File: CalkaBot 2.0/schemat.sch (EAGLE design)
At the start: 52 parts, among them IC1 TB6612FNG, IC2 LM339D, IC3 7806DT, Q1 16MHz

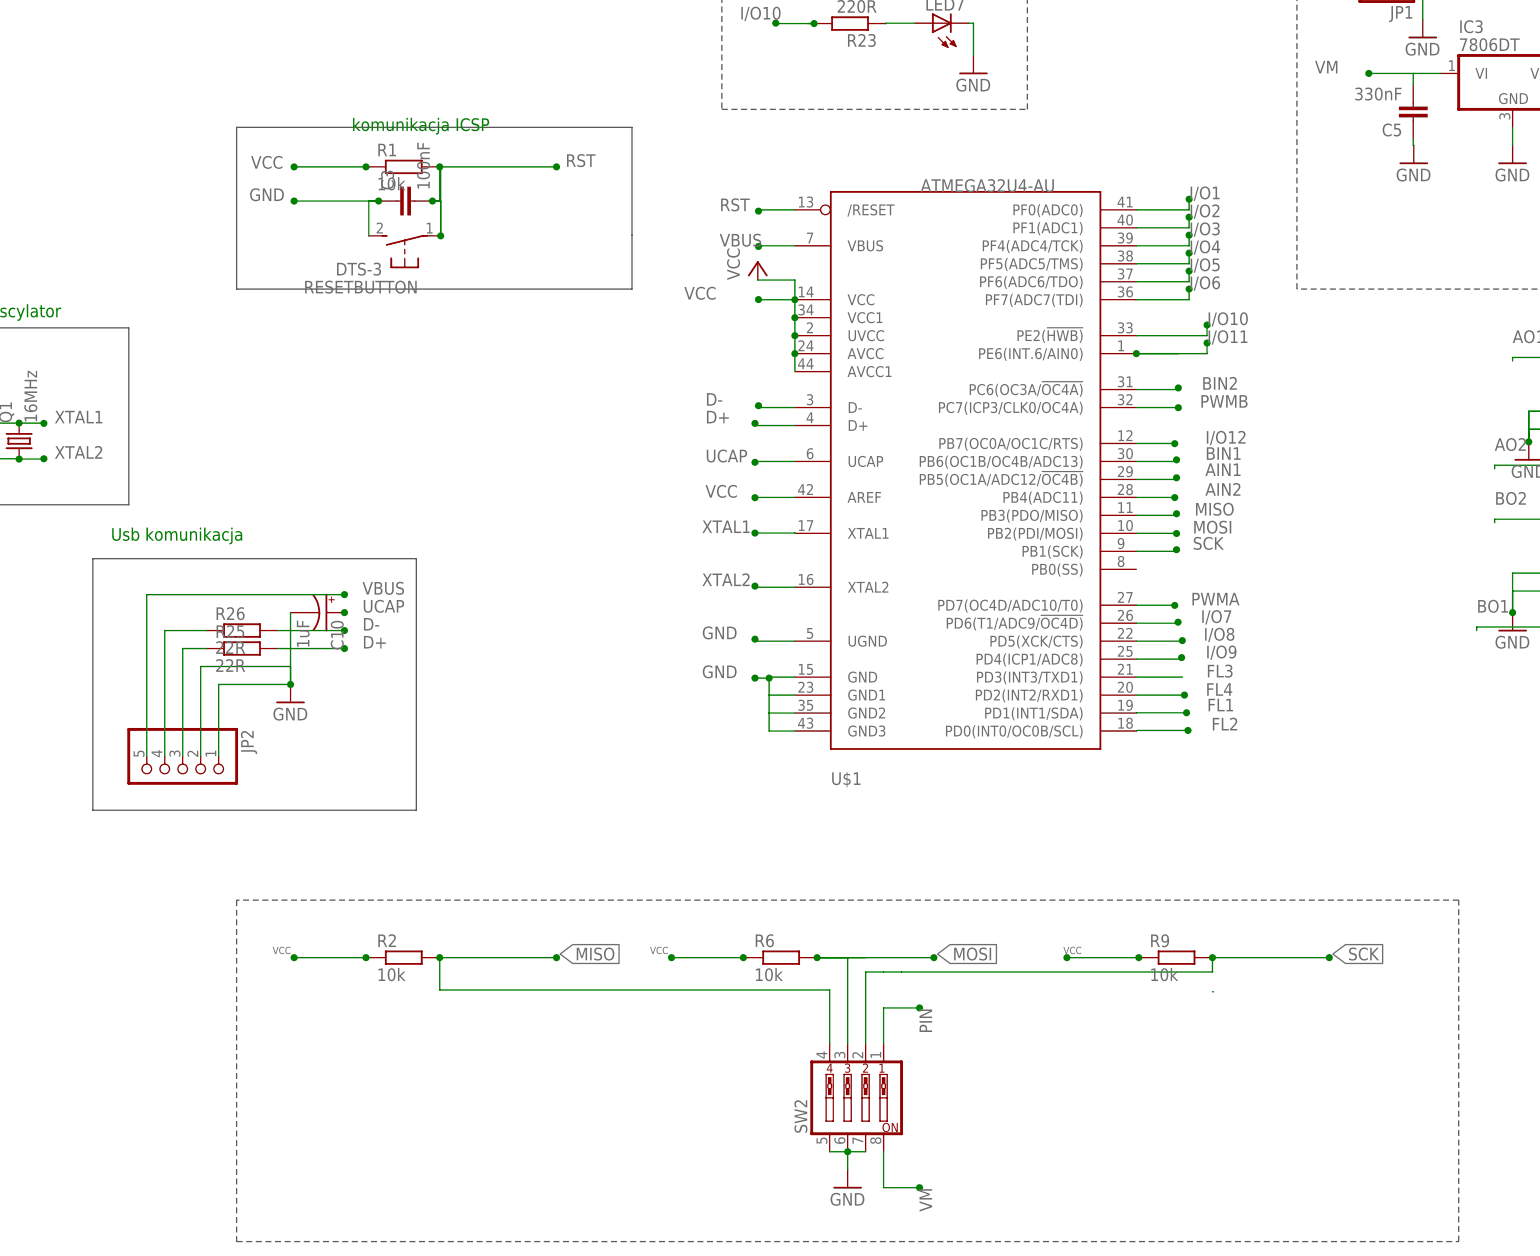
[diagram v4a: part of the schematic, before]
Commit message: dodałem gniazdo B, włącznik przyłączony z trybami
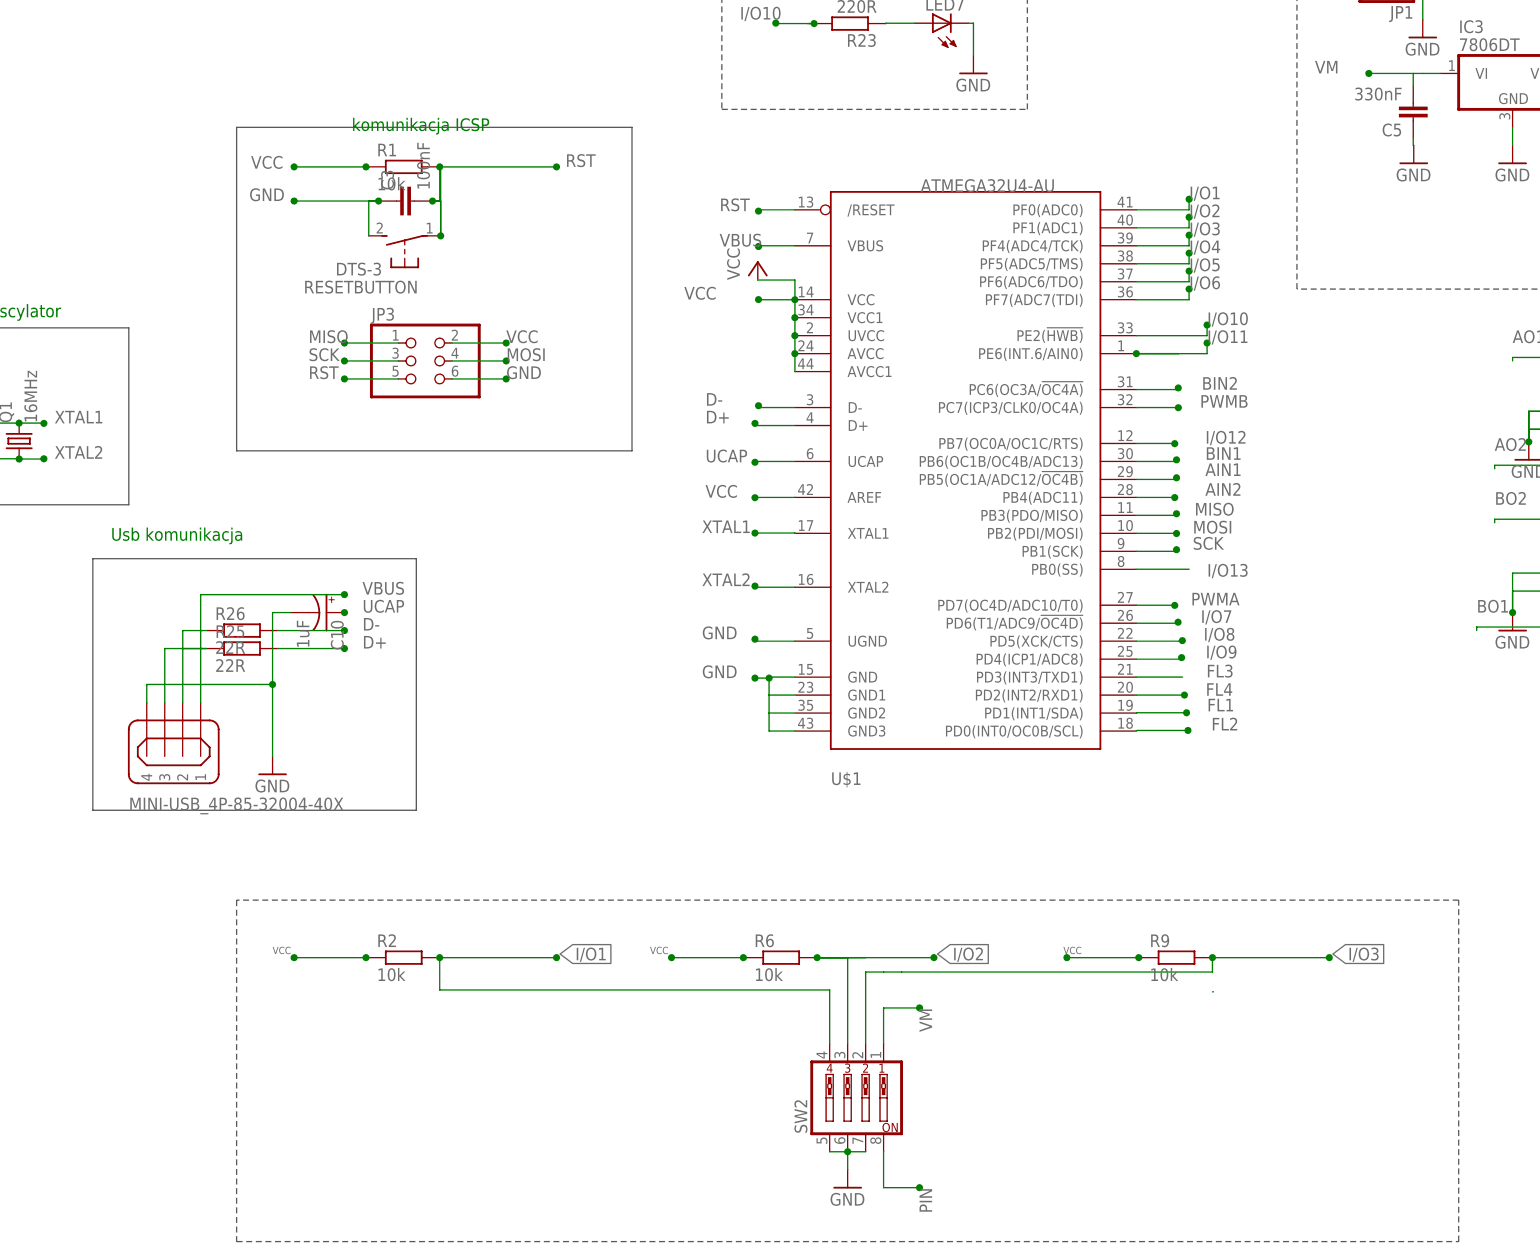
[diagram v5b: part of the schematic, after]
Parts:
- removed JP2: (no value), pinhead:PINHD-1X5
- added JP3: (no value), pinhead:PINHD-2X3
- added X1: MINI-USB_4P-85-32004-40X, con-cypressindustries:MINI-USB_4P-85-32004-40X
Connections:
- new net I/O13: U$1.PB0(SS)
- net GND: now also JP3.6, X1.4; no longer JP2.1, JP2.2
- net I/O1: now also R2.2, SW2.4
- net I/O2: now also R6.2, SW2.3
- net I/O3: now also R9.2, SW2.2
- net MISO: now also JP3.1; no longer R2.2, SW2.4
- net MOSI: now also JP3.4; no longer R6.2, SW2.3
- net N$11: now also X1.2; no longer JP2.4
- net N$12: now also X1.3; no longer JP2.3
- net PIN: now also SW2.8; no longer SW2.1
- net RST: now also JP3.5
- net SCK: now also JP3.3; no longer R9.2, SW2.2
- net VBUS: now also X1.1; no longer JP2.5
- net VCC: now also JP3.2
- net VM: now also SW2.1; no longer SW2.8

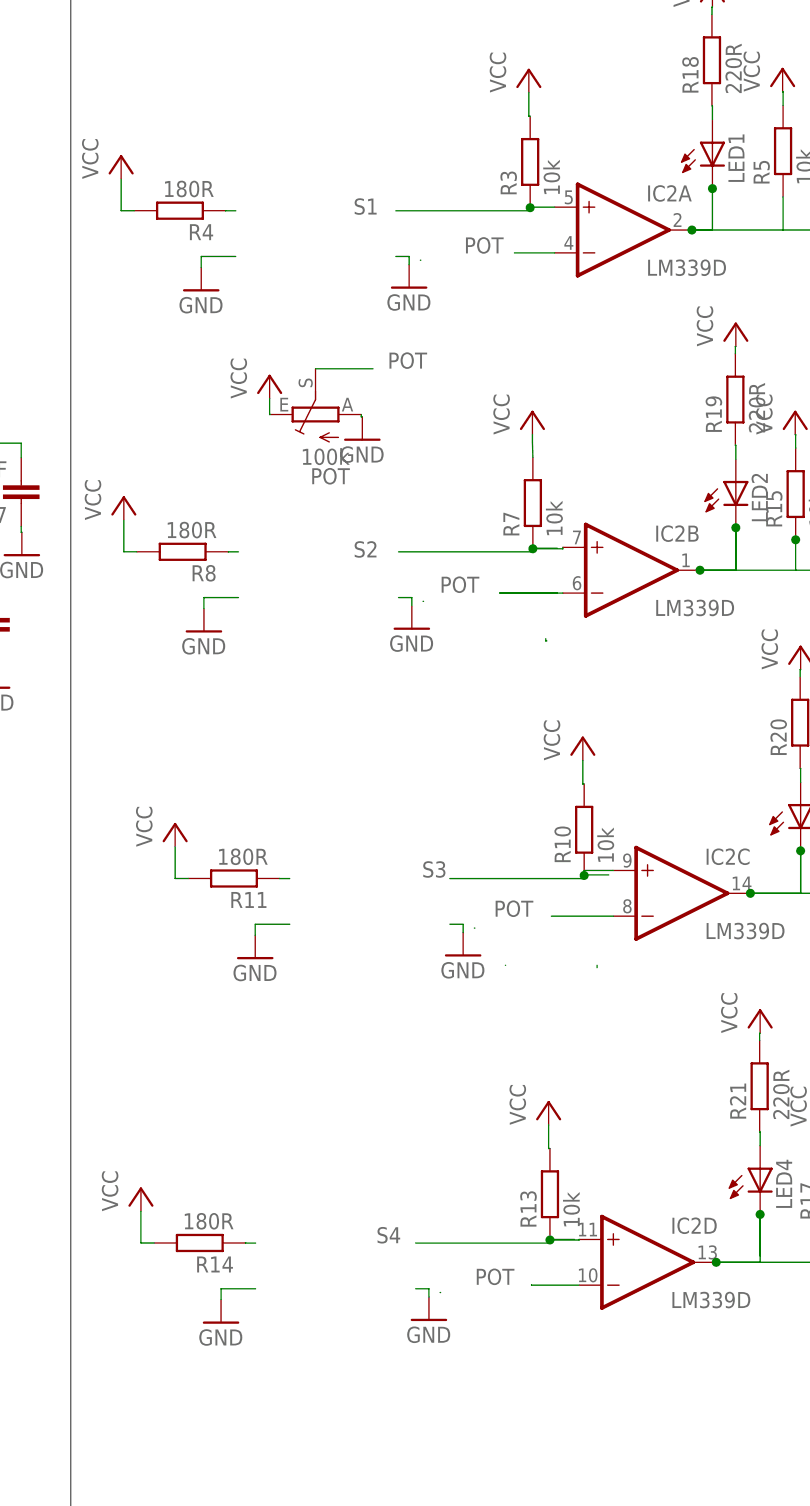
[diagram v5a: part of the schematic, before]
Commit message: dodałem koła i poczne ściany
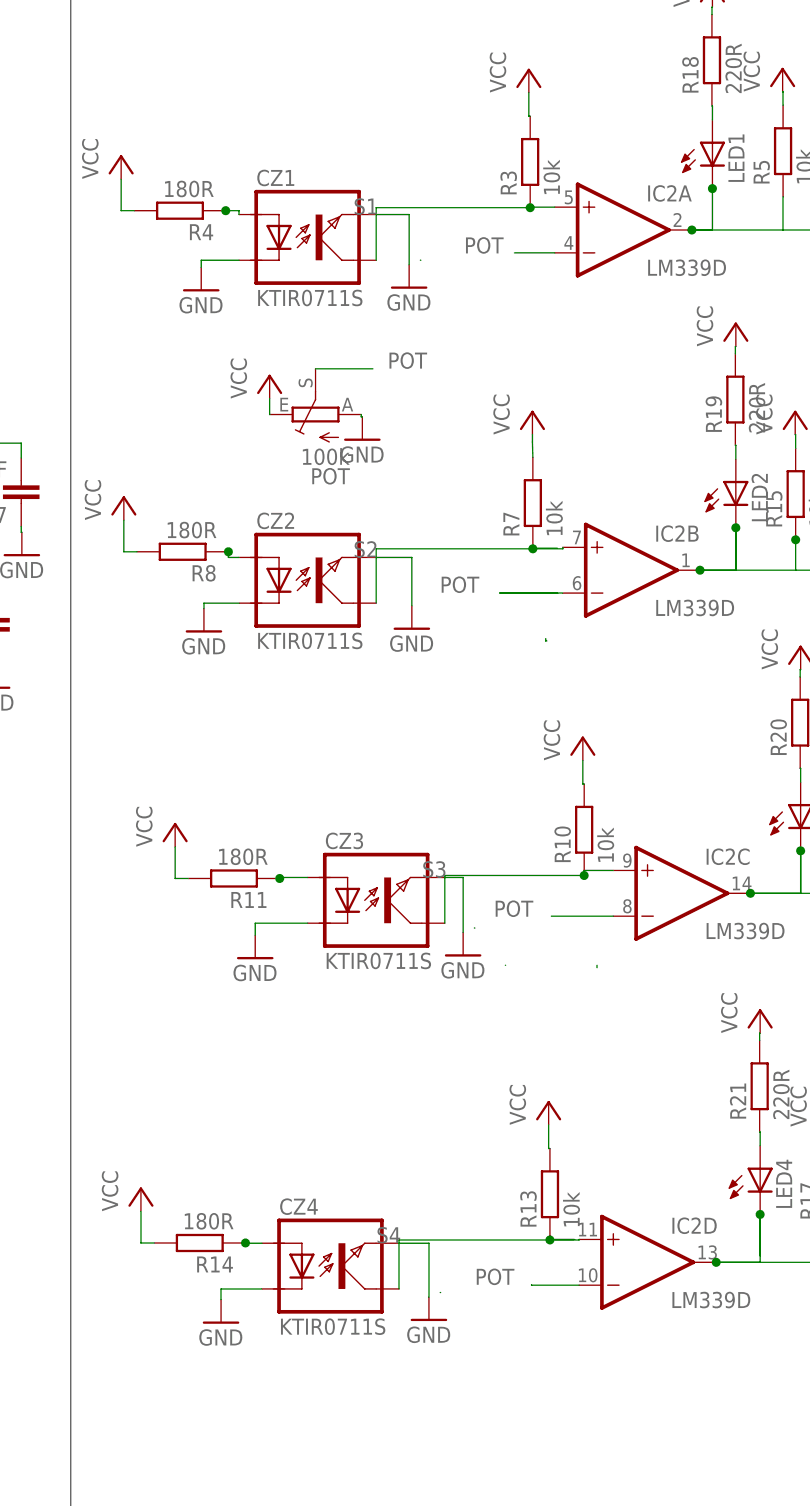
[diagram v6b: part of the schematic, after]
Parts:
- added CZ1, CZ2, CZ3, CZ4: KTIR0711S, ktir0711s:KTIR0711S
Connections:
- net GND: now also CZ1.EMITER, CZ1.KATODA, CZ2.EMITER, CZ2.KATODA, CZ3.EMITER, CZ3.KATODA, CZ4.EMITER, CZ4.KATODA
- net N$1: now also CZ1.ANODA
- net N$19: now also CZ2.ANODA
- net N$23: now also CZ3.ANODA
- net N$27: now also CZ4.ANODA
- net S1: now also CZ1.KOLEKTOR
- net S2: now also CZ2.KOLEKTOR
- net S3: now also CZ3.KOLEKTOR
- net S4: now also CZ4.KOLEKTOR
